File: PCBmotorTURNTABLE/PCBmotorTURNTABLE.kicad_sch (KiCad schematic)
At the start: 41 parts, among them J1 USB_C_Receptacle_USB2.0_16P, J10 Conn_01x04_Pin, J11 Conn_01x02_Pin, J12 Screw_Terminal_01x02, J2 USB_C_Receptacle_USB2.0_16P, J3 Conn_01x15_Pin, J4 Screw_Terminal_01x02, J5 Screw_Terminal_01x02, J6 Conn_01x15_Pin, J7 Conn_01x04_Pin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

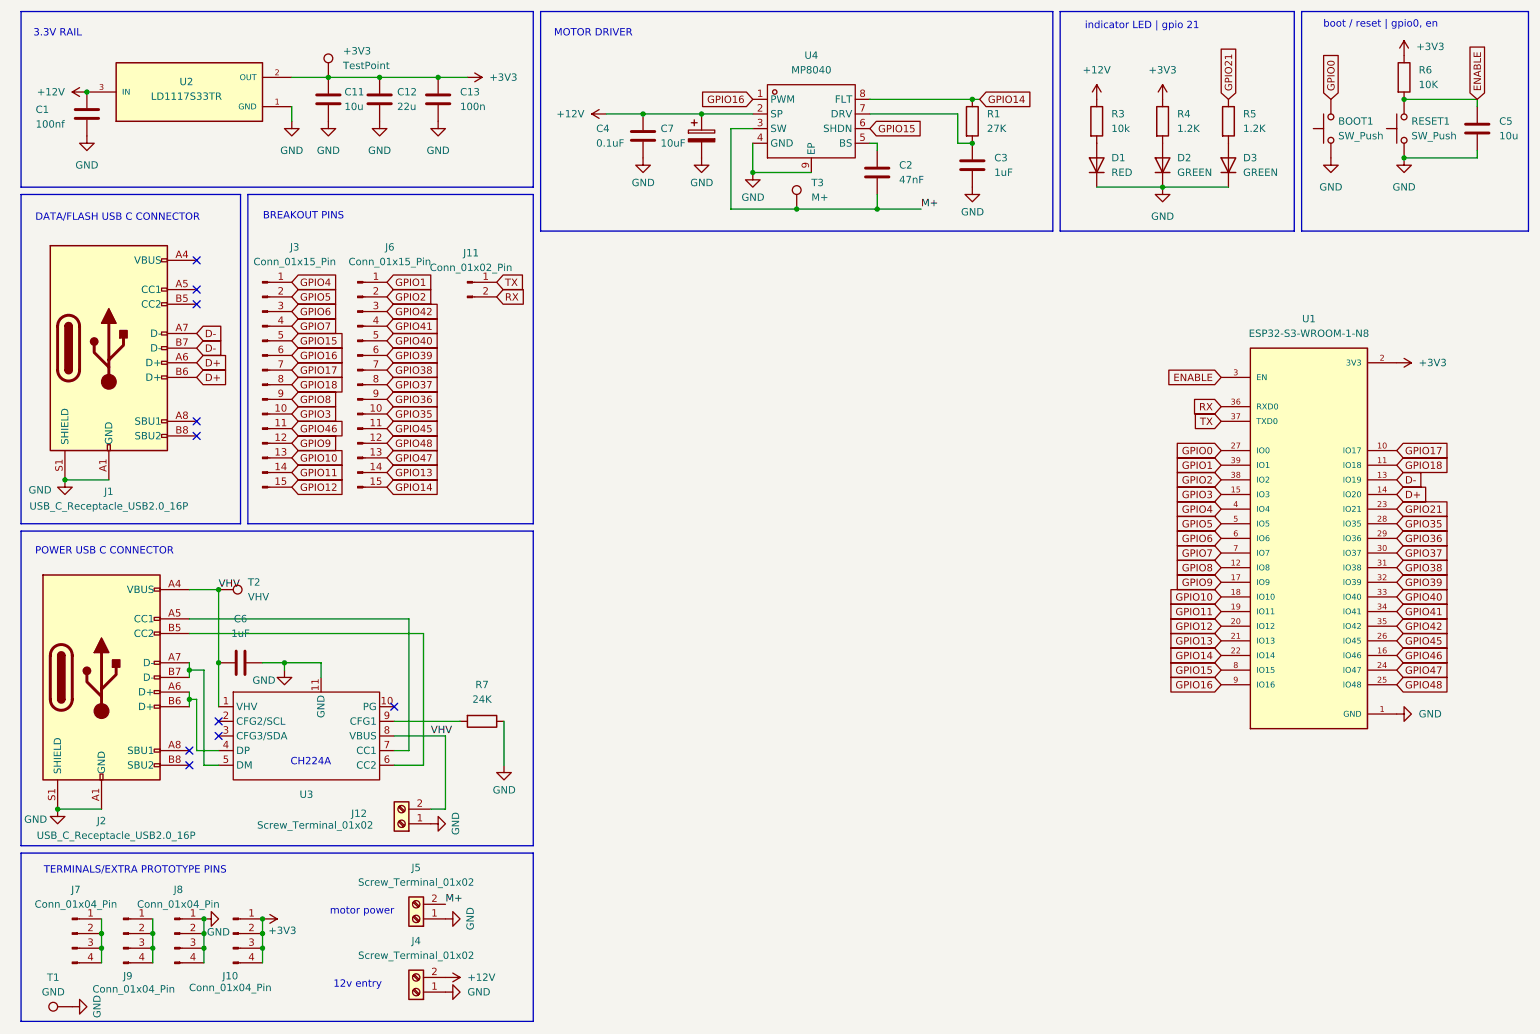
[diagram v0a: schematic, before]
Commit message: pcb->buckedit
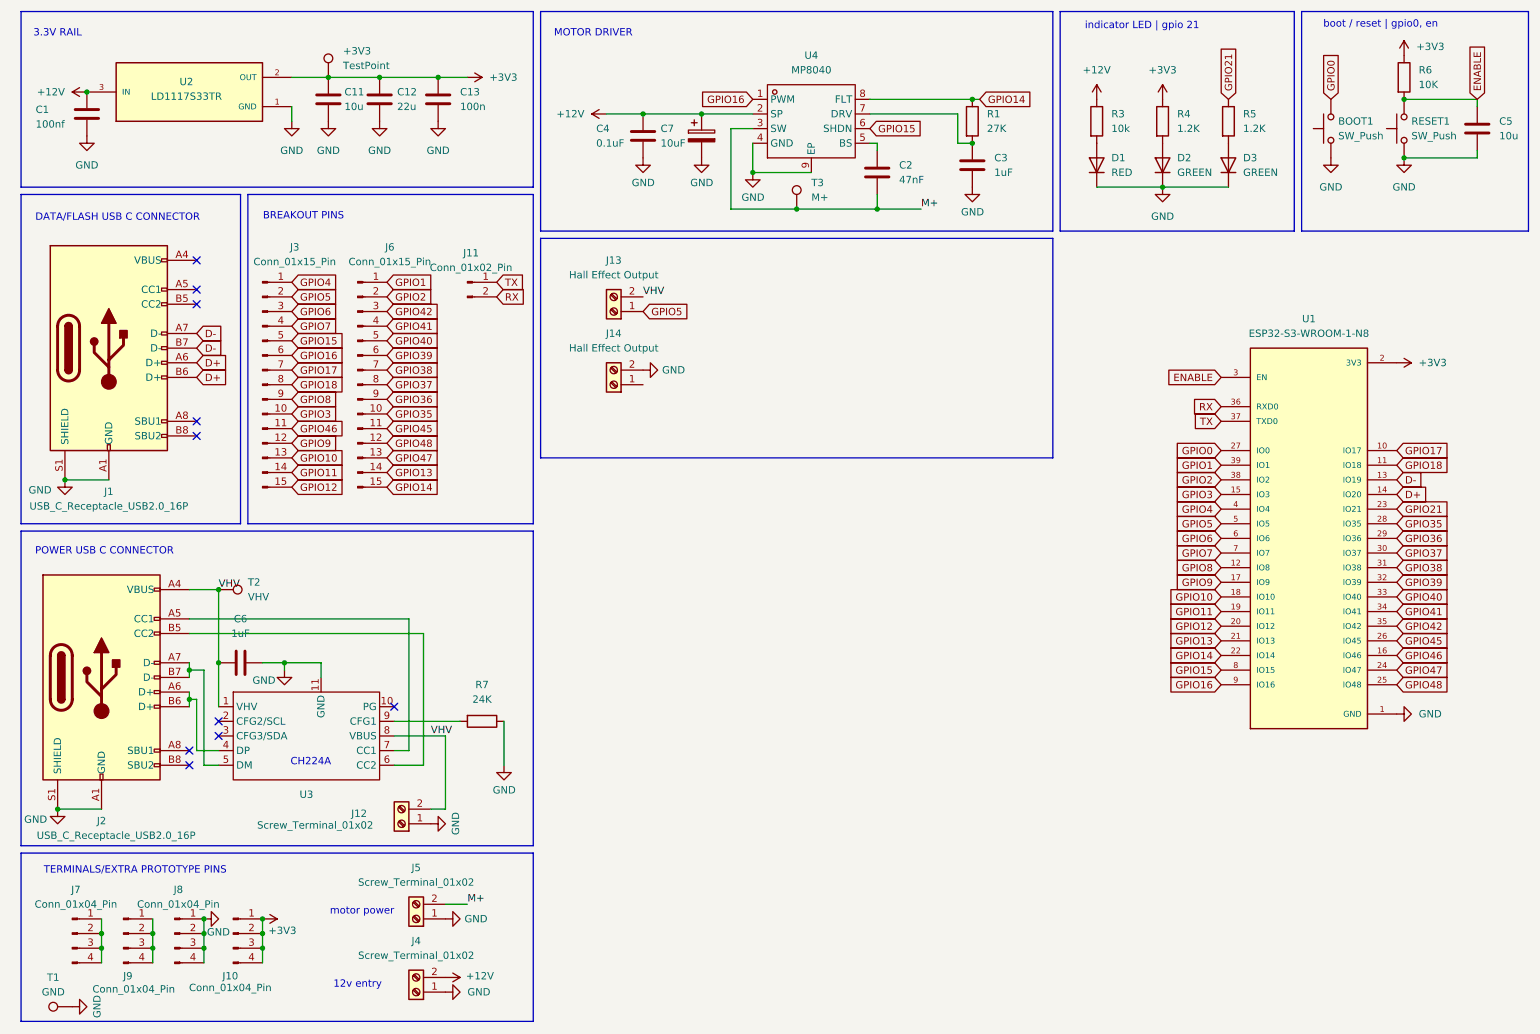
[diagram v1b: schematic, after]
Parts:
- added J13, J14: Hall Effect Output, TerminalBlock:TerminalBlock_MaiXu_MX126-5.0-02P_1x02_P5.00mm, symbol Connector:Screw_Terminal_01x02
- U1: DESCRIPTION Bluetooth, WiFi 802.11b/g/n, Bluetooth v5.0 Transceiver Mod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 -> (none)
- U3: value ~ -> (none)
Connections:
- net GND: now also J14.2 (Pin_2)
- net GPIO5: now also J13.1 (Pin_1)
- net VHV: now also J13.2 (Pin_2)
